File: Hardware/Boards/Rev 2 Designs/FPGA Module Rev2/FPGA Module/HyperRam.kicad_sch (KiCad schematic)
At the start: 40 parts, among them U12 W959D6NFKX4I, U14 W959D6NFKX4I, U16 W959D6NFKX4I, U6 W959D6NFKX4I

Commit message: FPGA Module Rev 2 Layout Begun
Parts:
- renumbered C98 to C117, C97 to C118, C96 to C119, C106 to C120, C107 to C121, C108 to C122, C100 to C123, C101 to C124, C103 to C125, C109 to C126, C111 to C127, C112 to C128, C99 to C129, C104 to C130, C105 to C131, C113 to C132, C114 to C133, C115 to C134, C116 to C135, C117 to C136, C136 to C137, C139 to C138, C187 to C139, C188 to C140, C189 to C141, C190 to C142, C191 to C143, C192 to C144, C193 to C145, C194 to C146, C195 to C147, C196 to C148, C197 to C149, C198 to C150, C199 to C151, C200 to C152, U6 to U14, U12 to U15, U14 to U16, U16 to U17

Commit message: Rev 2 PCB's and Heatsink PCB's complete
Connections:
- no-connect marks 4 -> 0
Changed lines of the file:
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@@
 		(color 0 0 0 0)
 	)
-	(no_connect
-		(at 137.16 118.11)
-	)
-	(no_connect
-		(at 306.07 232.41)
-	)
-	(no_connect
-		(at 137.16 232.41)
-	)
-	(no_connect
-		(at 306.07 118.11)
-	)
 	(bus_entry
 		(at 90.17 64.77)
@@
 			)
 		)
-		(pin "D7"
-		)
 		(pin "B3"
 		)
 		(pin "D2"
 		)
-		(pin "B1"
-		)
 		(pin "D1"
 		)
@@
 		(pin "E6"
 		)
-		(pin "E7"
-		)
 		(pin "E4"
 		)
@@
 		(pin "E3"
 		)
-		(pin "A2"
-		)
 		(pin "C1"
 		)
-		(pin "C3"
-		)
 		(pin "B7"
 		)
@@
 		(pin "C2"
 		)
-		(pin "B6"
-		)
 		(pin "D5"
 		)
 		(pin "C5"
 		)
-		(pin "A1"
-		)
-		(pin "C6"
-		)
 		(pin "D3"
 		)
 		(pin "B2"
 		)
-		(pin "A3"
-		)
 		(pin "F1"
 		)
@@
 		(pin "D4"
 		)
-		(pin "G4"
-		)
 		(pin "G5"
 		)
@@
 		(pin "A7"
 		)
-		(pin "A6"
-		)
 		(instances
 			(project "FPGA Module"
@@
 			)
 		)
-		(pin "D7"
-		)
 		(pin "B3"
 		)
 		(pin "D2"
 		)
-		(pin "B1"
-		)
 		(pin "D1"
 		)
@@
 		(pin "E6"
 		)
-		(pin "E7"
-		)
 		(pin "E4"
 		)
@@
 		(pin "E3"
 		)
-		(pin "A2"
-		)
 		(pin "C1"
 		)
-		(pin "C3"
-		)
 		(pin "B7"
 		)
@@
 		(pin "C2"
 		)
-		(pin "B6"
-		)
 		(pin "D5"
 		)
 		(pin "C5"
 		)
-		(pin "A1"
-		)
-		(pin "C6"
-		)
 		(pin "D3"
 		)
 		(pin "B2"
 		)
-		(pin "A3"
-		)
 		(pin "F1"
 		)
@@
 		(pin "D4"
 		)
-		(pin "G4"
-		)
 		(pin "G5"
 		)
@@
 		(pin "A7"
 		)
-		(pin "A6"
-		)
 		(instances
 			(project "FPGA Module"
@@
 			)
 		)
-		(pin "D7"
-		)
 		(pin "B3"
 		)
 		(pin "D2"
 		)
-		(pin "B1"
-		)
 		(pin "D1"
 		)
@@
 		(pin "E6"
 		)
-		(pin "E7"
-		)
 		(pin "E4"
 		)
@@
 		(pin "E3"
 		)
-		(pin "A2"
-		)
 		(pin "C1"
 		)
-		(pin "C3"
-		)
 		(pin "B7"
 		)
@@
 		(pin "C2"
 		)
-		(pin "B6"
-		)
 		(pin "D5"
 		)
 		(pin "C5"
 		)
-		(pin "A1"
-		)
-		(pin "C6"
-		)
 		(pin "D3"
 		)
 		(pin "B2"
 		)
-		(pin "A3"
-		)
 		(pin "F1"
 		)
@@
 		(pin "D4"
 		)
-		(pin "G4"
-		)
 		(pin "G5"
 		)
@@
 		(pin "A7"
 		)
-		(pin "A6"
-		)
 		(instances
 			(project "FPGA Module"
@@
 			)
 		)
-		(pin "D7"
-		)
 		(pin "B3"
 		)
 		(pin "D2"
 		)
-		(pin "B1"
-		)
 		(pin "D1"
 		)
@@
 		(pin "E6"
 		)
-		(pin "E7"
-		)
 		(pin "E4"
 		)
@@
 		(pin "E3"
 		)
-		(pin "A2"
-		)
 		(pin "C1"
 		)
-		(pin "C3"
-		)
 		(pin "B7"
 		)
@@
 		(pin "C2"
 		)
-		(pin "B6"
-		)
 		(pin "D5"
 		)
 		(pin "C5"
 		)
-		(pin "A1"
-		)
-		(pin "C6"
-		)
 		(pin "D3"
 		)
 		(pin "B2"
 		)
-		(pin "A3"
-		)
 		(pin "F1"
 		)
@@
 		(pin "D4"
 		)
-		(pin "G4"
-		)
 		(pin "G5"
 		)
@@
 		(pin "A7"
 		)
-		(pin "A6"
-		)
 		(instances

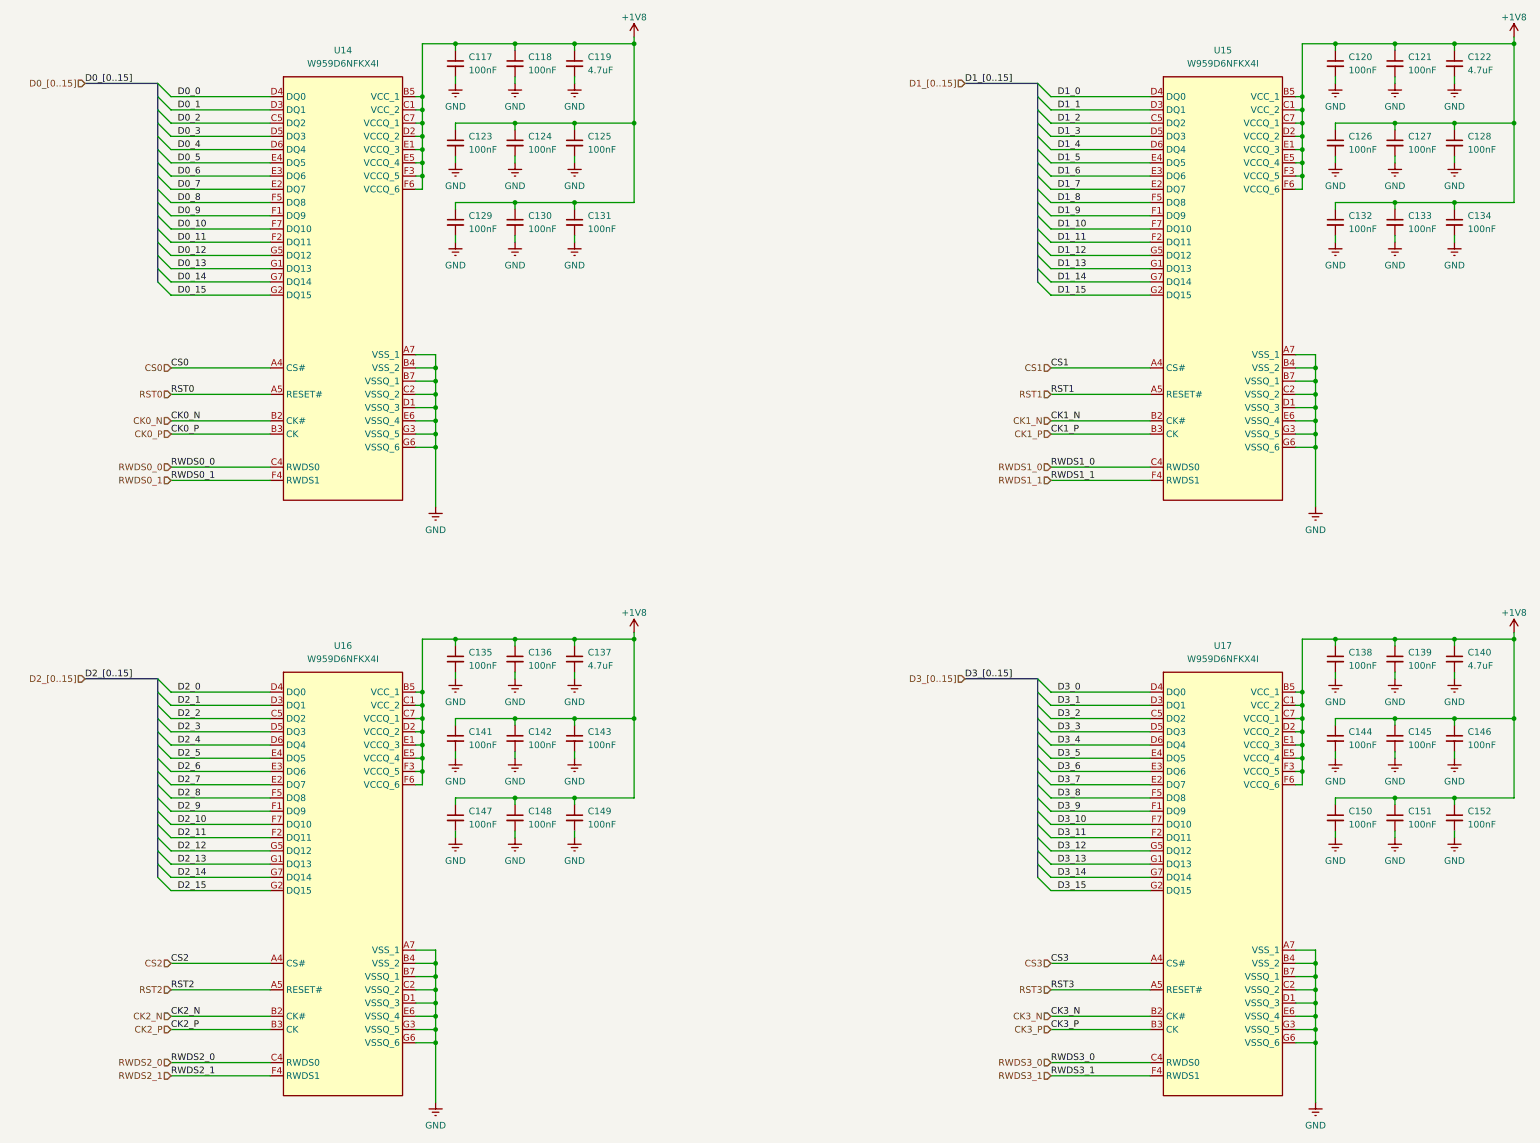
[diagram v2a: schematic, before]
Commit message: modified FPGA MIPI code to add ready output, modified IO module FW to initialize camera after fpga rdy goes high
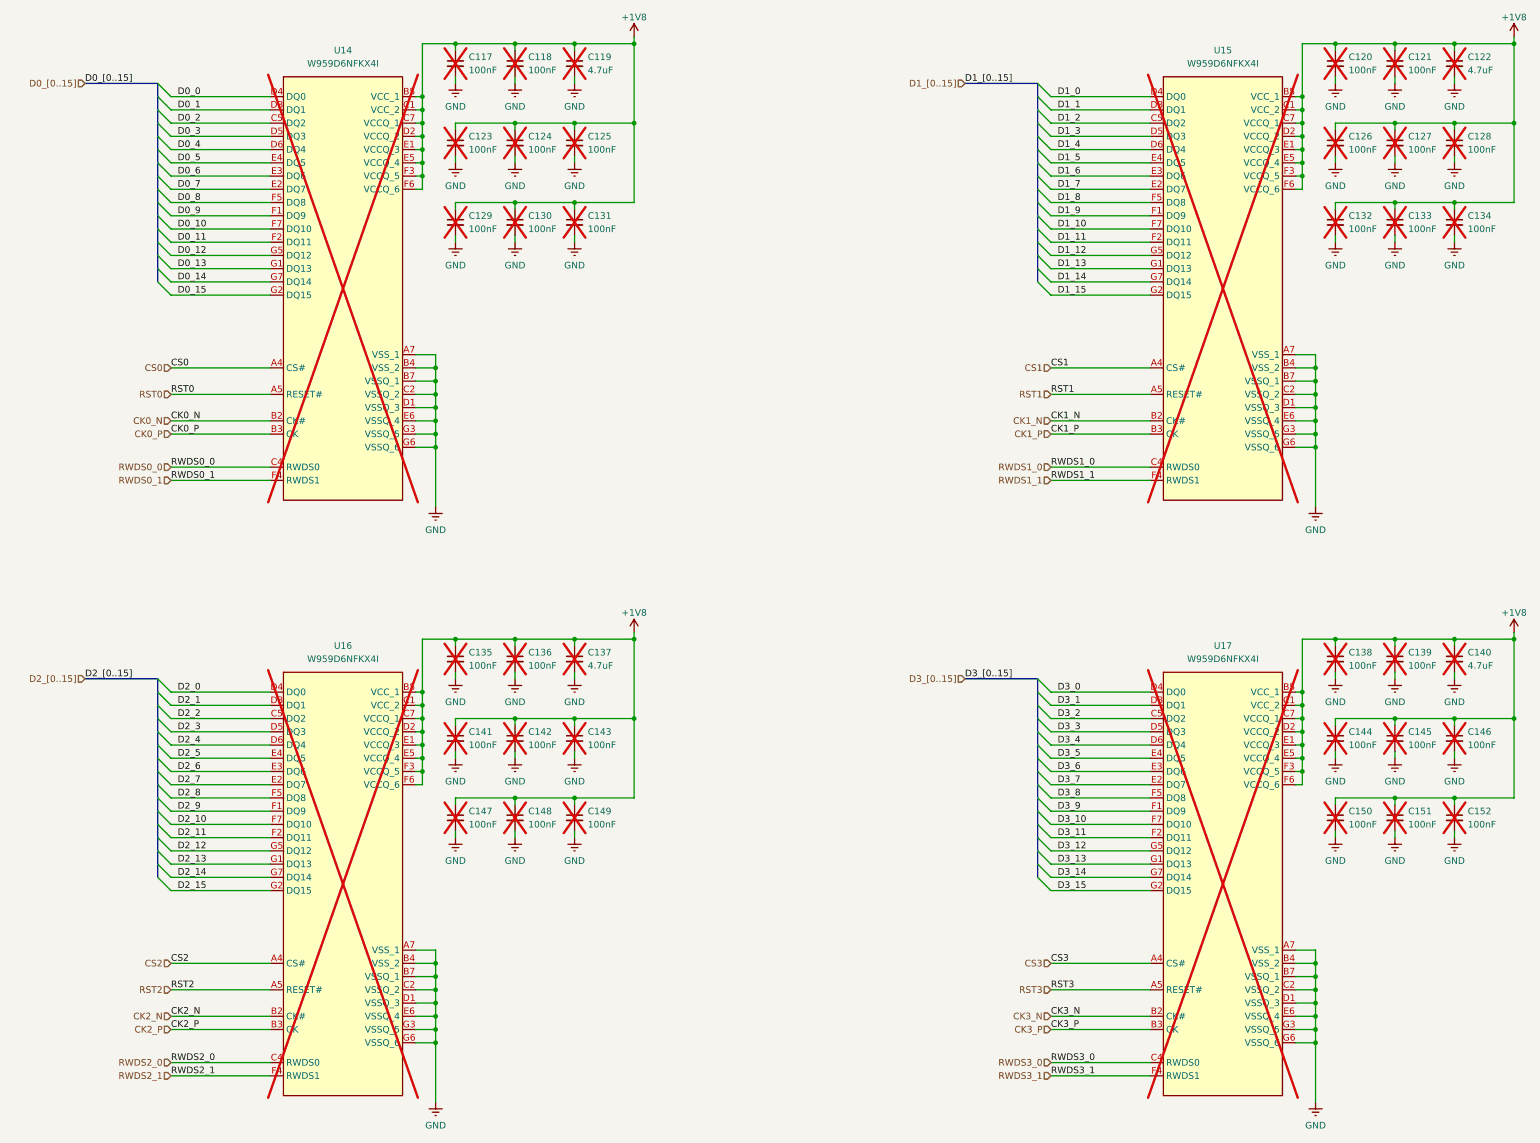
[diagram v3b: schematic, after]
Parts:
- C117, C118, C119, C120, C121, C122, C123, C124, C125, C126, C127, C128, C129, C130, C131, C132, C133, C134, C135, C136, C137, C138, C139, C140, C141, C142, C143, C144, C145, C146, C147, C148, C149, C150, C151, C152, U14, U15, U16, U17: now not fitted
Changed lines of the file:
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@@
 		(in_bom yes)
 		(on_board yes)
-		(dnp no)
+		(dnp yes)
 		(fields_autoplaced yes)
 		(property "Reference" "U15"
@@
 		(in_bom yes)
 		(on_board yes)
-		(dnp no)
+		(dnp yes)
 		(fields_autoplaced yes)
 		(property "Reference" "C118"
@@
 		(in_bom yes)
 		(on_board yes)
-		(dnp no)
+		(dnp yes)
 		(fields_autoplaced yes)
 		(property "Reference" "C136"
@@
 		(in_bom yes)
 		(on_board yes)
-		(dnp no)
+		(dnp yes)
 		(fields_autoplaced yes)
 		(property "Reference" "C147"
@@
 		(in_bom yes)
 		(on_board yes)
-		(dnp no)
+		(dnp yes)
 		(fields_autoplaced yes)
 		(property "Reference" "C135"
@@
 		(in_bom yes)
 		(on_board yes)
-		(dnp no)
+		(dnp yes)
 		(fields_autoplaced yes)
 		(property "Reference" "C144"
@@
 		(in_bom yes)
 		(on_board yes)
-		(dnp no)
+		(dnp yes)
 		(fields_autoplaced yes)
 		(property "Reference" "U16"
@@
 		(in_bom yes)
 		(on_board yes)
-		(dnp no)
+		(dnp yes)
 		(fields_autoplaced yes)
 		(property "Reference" "C117"
@@
 		(in_bom yes)
 		(on_board yes)
-		(dnp no)
+		(dnp yes)
 		(fields_autoplaced yes)
 		(property "Reference" "C131"
@@
 		(in_bom yes)
 		(on_board yes)
-		(dnp no)
+		(dnp yes)
 		(fields_autoplaced yes)
 		(property "Reference" "C148"
@@
 		(in_bom yes)
 		(on_board yes)
-		(dnp no)
+		(dnp yes)
 		(fields_autoplaced yes)
 		(property "Reference" "U17"
@@
 		(in_bom yes)
 		(on_board yes)
-		(dnp no)
+		(dnp yes)
 		(fields_autoplaced yes)
 		(property "Reference" "C120"
@@
 		(in_bom yes)
 		(on_board yes)
-		(dnp no)
+		(dnp yes)
 		(fields_autoplaced yes)
 		(property "Reference" "U14"
@@
 		(in_bom yes)
 		(on_board yes)
-		(dnp no)
+		(dnp yes)
 		(fields_autoplaced yes)
 		(property "Reference" "C126"
@@
 		(in_bom yes)
 		(on_board yes)
-		(dnp no)
+		(dnp yes)
 		(fields_autoplaced yes)
 		(property "Reference" "C128"
@@
 		(in_bom yes)
 		(on_board yes)
-		(dnp no)
+		(dnp yes)
 		(fields_autoplaced yes)
 		(property "Reference" "C149"
@@
 		(in_bom yes)
 		(on_board yes)
-		(dnp no)
+		(dnp yes)
 		(fields_autoplaced yes)
 		(property "Reference" "C132"
@@
 		(in_bom yes)
 		(on_board yes)
-		(dnp no)
+		(dnp yes)
 		(fields_autoplaced yes)
 		(property "Reference" "C142"
@@
 		(in_bom yes)
 		(on_board yes)
-		(dnp no)
+		(dnp yes)
 		(fields_autoplaced yes)
 		(property "Reference" "C134"
@@
 		(in_bom yes)
 		(on_board yes)
-		(dnp no)
+		(dnp yes)
 		(fields_autoplaced yes)
 		(property "Reference" "C138"
@@
 		(in_bom yes)
 		(on_board yes)
-		(dnp no)
+		(dnp yes)
 		(fields_autoplaced yes)
 		(property "Reference" "C124"
@@
 		(in_bom yes)
 		(on_board yes)
-		(dnp no)
+		(dnp yes)
 		(fields_autoplaced yes)
 		(property "Reference" "C140"
@@
 		(in_bom yes)
 		(on_board yes)
-		(dnp no)
+		(dnp yes)
 		(fields_autoplaced yes)
 		(property "Reference" "C127"
@@
 		(in_bom yes)
 		(on_board yes)
-		(dnp no)
+		(dnp yes)
 		(fields_autoplaced yes)
 		(property "Reference" "C125"
@@
 		(in_bom yes)
 		(on_board yes)
-		(dnp no)
+		(dnp yes)
 		(fields_autoplaced yes)
 		(property "Reference" "C122"
@@
 		(in_bom yes)
 		(on_board yes)
-		(dnp no)
+		(dnp yes)
 		(fields_autoplaced yes)
 		(property "Reference" "C130"
@@
 		(in_bom yes)
 		(on_board yes)
-		(dnp no)
+		(dnp yes)
 		(fields_autoplaced yes)
 		(property "Reference" "C119"
@@
 		(in_bom yes)
 		(on_board yes)
-		(dnp no)
+		(dnp yes)
 		(fields_autoplaced yes)
 		(property "Reference" "C145"
@@
 		(in_bom yes)
 		(on_board yes)
-		(dnp no)
+		(dnp yes)
 		(fields_autoplaced yes)
 		(property "Reference" "C123"
@@
 		(in_bom yes)
 		(on_board yes)
-		(dnp no)
+		(dnp yes)
 		(fields_autoplaced yes)
 		(property "Reference" "C152"
@@
 		(in_bom yes)
 		(on_board yes)
-		(dnp no)
+		(dnp yes)
 		(fields_autoplaced yes)
 		(property "Reference" "C146"
@@
 		(in_bom yes)
 		(on_board yes)
-		(dnp no)
+		(dnp yes)
 		(fields_autoplaced yes)
 		(property "Reference" "C121"
@@
 		(in_bom yes)
 		(on_board yes)
-		(dnp no)
+		(dnp yes)
 		(fields_autoplaced yes)
 		(property "Reference" "C139"
@@
 		(in_bom yes)
 		(on_board yes)
-		(dnp no)
+		(dnp yes)
 		(fields_autoplaced yes)
 		(property "Reference" "C151"
@@
 		(in_bom yes)
 		(on_board yes)
-		(dnp no)
+		(dnp yes)
 		(fields_autoplaced yes)
 		(property "Reference" "C143"
@@
 		(in_bom yes)
 		(on_board yes)
-		(dnp no)
+		(dnp yes)
 		(fields_autoplaced yes)
 		(property "Reference" "C133"
@@
 		(in_bom yes)
 		(on_board yes)
-		(dnp no)
+		(dnp yes)
 		(fields_autoplaced yes)
 		(property "Reference" "C129"
@@
 		(in_bom yes)
 		(on_board yes)
-		(dnp no)
+		(dnp yes)
 		(fields_autoplaced yes)
 		(property "Reference" "C150"
@@
 		(in_bom yes)
 		(on_board yes)
-		(dnp no)
+		(dnp yes)
 		(fields_autoplaced yes)
 		(property "Reference" "C141"
@@
 		(in_bom yes)
 		(on_board yes)
-		(dnp no)
+		(dnp yes)
 		(fields_autoplaced yes)
 		(property "Reference" "C137"

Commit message: Added diagrams, papers and presentations
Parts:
- C117, C118, C119, C120, C121, C122, C123, C124, C125, C126, C127, C128, C129, C130, C131, C132, C133, C134, C135, C136, C137, C138, C139, C140, C141, C142, C143, C144, C145, C146, C147, C148, C149, C150, C151, C152, U14, U15, U16, U17: now fitted
